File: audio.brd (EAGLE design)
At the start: 64.8 x 36.8 mm, 42 parts, among them CN1 PH-1X06SG, CN2 PH-1X06RG, CN3 STEREO-3.5-MJ8435, CN4 STEREO-3.5-MJ8435, CN5 DC-JACK-18742, IC1 R5F104BCAFP, IC2 NJM2746E, IC3 NJM2746E, IC4 VBT1-S5-S5-SMT, IC5 NJM2866F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

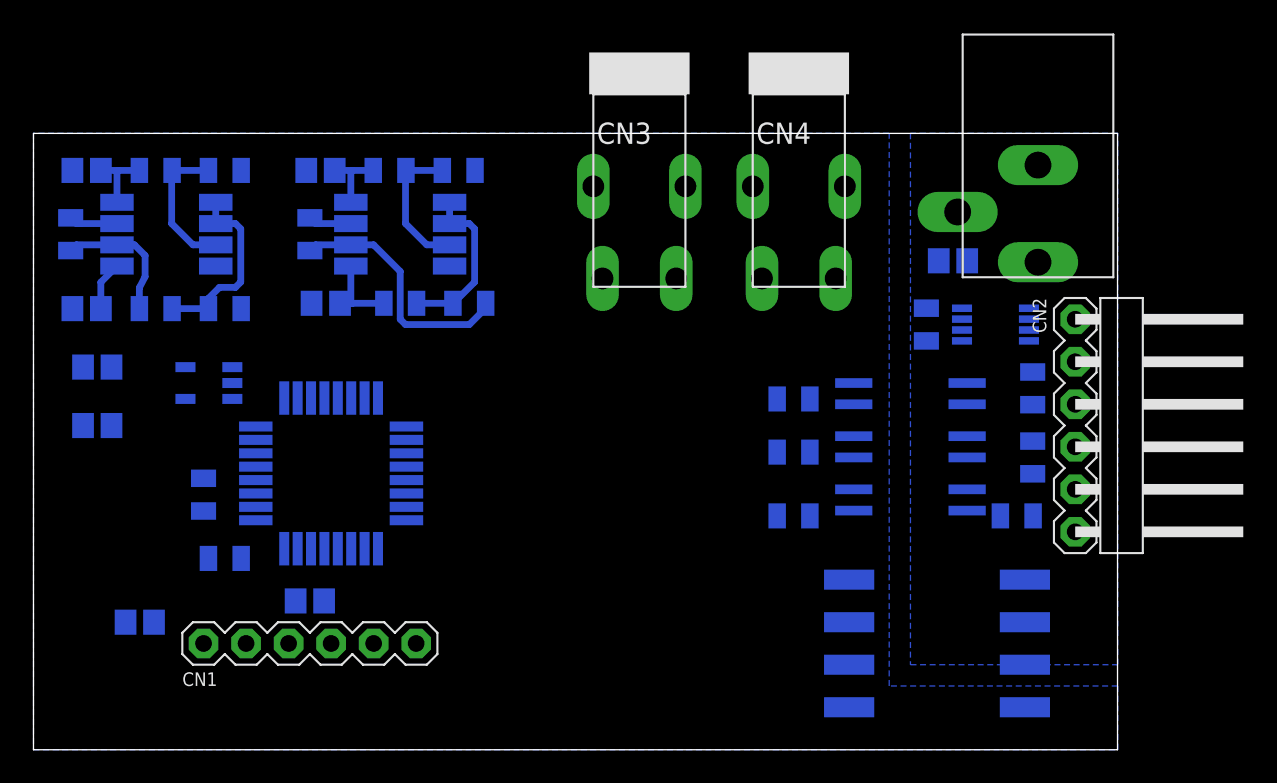
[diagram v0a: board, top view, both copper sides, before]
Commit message: Added power chains
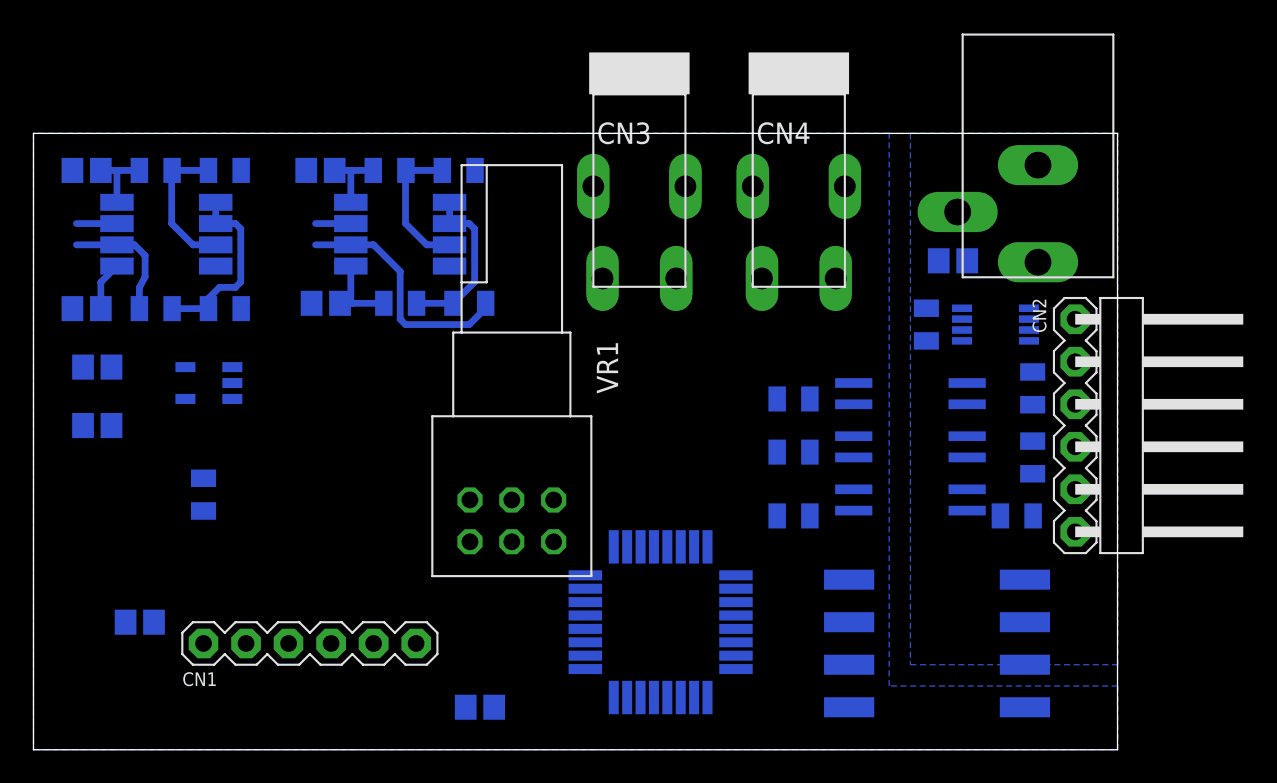
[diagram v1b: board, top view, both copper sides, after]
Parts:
- removed IC1: R5F104BCAFP, MyLib:P-LQFP32-7X7-0.80
- removed R1: 4.7k, MyLib:R2012
- removed R11, R12: 10k, MyLib:R2012
- added IC7: STM32F303K8T6, MyLib:P-LQFP32-7X7-0.80
- added VR1: (no value), MyLib:RK0971220-F15-C0-A104
- C1: value 1u -> 0.1u
- moved C1 12.0 mm to (26.7, 2.54)
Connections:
- net +3V3: now also C1.1, IC7.1, IC7.17, IC7.5; no longer IC1.8, R1.1, R2.1
- net GND: now also IC7.16, IC7.32, R2.1; no longer IC1.3, IC1.4, IC1.5, IC1.7
- net N$10: now also VR1.A3; no longer IC1.28, R11.2
- net N$14: now also VR1.B2; no longer R12.1
- net N$16: now also VR1.B3; no longer IC1.29, R12.2
- net N$17: no longer IC1.24
- net N$18: no longer IC1.23
- net N$19: no longer IC1.22
- net N$2: now also IC7.31, R2.2; no longer C1.1, IC1.6
- net N$4: no longer IC1.16
- net N$9: now also VR1.A2; no longer R11.1
- net RESET: no longer IC1.2, R2.2
- net TOOL0: no longer IC1.1, IC1.15, R1.2
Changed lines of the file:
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@@
 </autorouter>
 <elements>
-<element name="C1" library="MyLib" package="C2012" value="1u" x="16.51" y="8.89" rot="MR0"/>
 <element name="C2" library="MyLib" package="C2012" value="0.1u" x="6.35" y="7.62" rot="MR0"/>
 <element name="CN2" library="MyLib" package="PH-1X06RG" value="PH-1X06RG" x="62.23" y="19.3675" rot="R270"/>
-<element name="IC1" library="MyLib" package="P-LQFP32-7X7-0.80" value="R5F104BCAFP" x="17.78" y="16.51" rot="MR0"/>
 <element name="IC2" library="MyLib" package="EMP8" value="NJM2746E" x="21.9075" y="30.7975" rot="MR0"/>
-<element name="R1" library="MyLib" package="R2012" value="4.7k" x="11.43" y="11.43" rot="MR0"/>
 <element name="R2" library="MyLib" package="R2012" value="47k" x="10.16" y="15.24" rot="MR270"/>
 <element name="CN3" library="MyLib" package="MJ8435" value="STEREO-3.5-MJ8435" x="36.195" y="33.655"/>
@@
 <element name="C7" library="MyLib" package="C2012" value="0.1u" x="3.175" y="34.6075" rot="MR0"/>
 <element name="C8" library="MyLib" package="C2012" value="0.1u" x="17.145" y="34.6075" rot="MR0"/>
-<element name="R11" library="MyLib" package="R2012" value="10k" x="16.51" y="30.7975" rot="MR90"/>
-<element name="R12" library="MyLib" package="R2012" value="10k" x="2.2225" y="30.7975" rot="MR90"/>
 <element name="R13" library="MyLib" package="R2012" value="1k" x="45.4025" y="17.78" rot="MR180"/>
 <element name="R14" library="MyLib" package="R2012" value="100" x="45.4025" y="20.955" rot="MR180"/>
@@
 <element name="C9" library="MyLib" package="C2012" value="0.1u" x="54.9275" y="29.21" rot="MR0"/>
 <element name="R19" library="MyLib" package="R2012" value="4.7k" x="59.69" y="17.4625" rot="MR270"/>
+<element name="VR1" library="MyLib" package="RK0971220-F15-C0-A104" value="" x="28.575" y="14.9225"/>
+<element name="IC7" library="MyLib" package="P-LQFP32-7X7-0.80" value="STM32F303K8T6" x="37.465" y="7.62" rot="MR0"/>
+<element name="C1" library="MyLib" package="C2012" value="0.1u" x="26.67" y="2.54" rot="MR0"/>
 </elements>
 <signals>
@@
 <wire x1="4.66" y1="22.86" x2="11.8775" y2="22.8575" width="0" layer="19" extent="16-16"/>
 </signal>
-<signal name="N$2">
-<contactref element="IC1" pad="6"/>
-<contactref element="C1" pad="1"/>
-<wire x1="17.36" y1="8.89" x2="16.58" y2="12.01" width="0" layer="19" extent="16-16"/>
-</signal>
 <signal name="GND">
-<contactref element="IC1" pad="7"/>
-<contactref element="C2" pad="2"/>
-<contactref element="C1" pad="2"/>
-<contactref element="IC1" pad="3"/>
-<contactref element="IC1" pad="4"/>
-<contactref element="IC1" pad="5"/>
 <contactref element="CN1" pad="P$6"/>
 <contactref element="IC5" pad="P$2"/>
@@
 <vertex x="0" y="36.83"/>
 </polygon>
+<contactref element="IC7" pad="32"/>
+<contactref element="IC7" pad="16"/>
+<contactref element="R2" pad="1"/>
+<contactref element="C2" pad="2"/>
+<contactref element="C1" pad="2"/>
 </signal>
 <signal name="N$4">
-<contactref element="IC1" pad="16"/>
 <contactref element="CN1" pad="P$2"/>
-<wire x1="12.7" y1="6.35" x2="13.28" y2="19.31" width="0" layer="19" extent="16-16"/>
 </signal>
 <signal name="TOOL0">
-<contactref element="IC1" pad="15"/>
-<contactref element="R1" pad="2"/>
-<contactref element="IC1" pad="1"/>
 <contactref element="CN1" pad="P$3"/>
-<wire x1="10.453" y1="11.43" x2="13.28" y2="18.51" width="0" layer="19" extent="16-16"/>
-<wire x1="15.24" y1="6.35" x2="10.453" y2="11.43" width="0" layer="19" extent="16-16"/>
-<wire x1="20.58" y1="12.01" x2="15.24" y2="6.35" width="0" layer="19" extent="16-16"/>
 </signal>
 <signal name="RESET">
-<contactref element="R2" pad="2"/>
-<contactref element="IC1" pad="2"/>
 <contactref element="CN1" pad="P$5"/>
-<wire x1="20.32" y1="6.35" x2="19.78" y2="12.01" width="0" layer="19" extent="16-16"/>
-<wire x1="10.16" y1="14.263" x2="19.78" y2="12.01" width="0" layer="19" extent="16-16"/>
 </signal>
 <signal name="N$3">
@@
 </signal>
 <signal name="+3V3">
-<contactref element="IC1" pad="8"/>
-<contactref element="C2" pad="1"/>
-<contactref element="R2" pad="1"/>
-<contactref element="R1" pad="1"/>
 <contactref element="IC5" pad="P$5"/>
 <contactref element="C6" pad="1"/>
@@
 <wire x1="4.9875" y1="32.7025" x2="4.9875" y2="34.515" width="0.4064" layer="16"/>
 <wire x1="4.9875" y1="34.515" x2="5.08" y2="34.6075" width="0.4064" layer="16"/>
-<wire x1="20.2955" y1="34.6075" x2="44.4255" y2="17.78" width="0" layer="19" extent="16-16"/>
-<wire x1="6.3255" y1="34.6075" x2="17.995" y2="34.6075" width="0" layer="19" extent="16-16"/>
-<wire x1="9.0775" y1="22.8575" x2="4.9875" y2="32.7025" width="0" layer="19" extent="16-16"/>
-<wire x1="4.66" y1="19.3675" x2="9.0775" y2="22.8575" width="0" layer="19" extent="16-16"/>
-<wire x1="10.16" y1="16.217" x2="4.66" y2="19.3675" width="0" layer="19" extent="16-16"/>
-<wire x1="12.407" y1="11.43" x2="10.16" y2="16.217" width="0" layer="19" extent="16-16"/>
-<wire x1="14.98" y1="12.01" x2="12.407" y2="11.43" width="0" layer="19" extent="16-16"/>
-<wire x1="7.2" y1="7.62" x2="12.407" y2="11.43" width="0" layer="19" extent="16-16"/>
+<contactref element="IC7" pad="1"/>
+<contactref element="IC7" pad="5"/>
+<contactref element="C2" pad="1"/>
+<contactref element="IC7" pad="17"/>
+<contactref element="C1" pad="1"/>
+<wire x1="34.665" y1="12.12" x2="44.4255" y2="17.78" width="0" layer="19" extent="16-16"/>
+<wire x1="37.065" y1="3.12" x2="34.665" y2="12.12" width="0" layer="19" extent="16-16"/>
+<wire x1="40.265" y1="3.12" x2="37.065" y2="3.12" width="0" layer="19" extent="16-16"/>
+<wire x1="27.52" y1="2.54" x2="37.065" y2="3.12" width="0" layer="19" extent="16-16"/>
+<wire x1="7.2" y1="7.62" x2="27.52" y2="2.54" width="0" layer="19" extent="16-16"/>
+<wire x1="4.66" y1="19.3675" x2="7.2" y2="7.62" width="0" layer="19" extent="16-16"/>
+<wire x1="9.0775" y1="22.8575" x2="4.66" y2="19.3675" width="0" layer="19" extent="16-16"/>
+<wire x1="4.9875" y1="32.7025" x2="9.0775" y2="22.8575" width="0" layer="19" extent="16-16"/>
+<wire x1="17.995" y1="34.6075" x2="6.3255" y2="34.6075" width="0" layer="19" extent="16-16"/>
 </signal>
 <signal name="N$7">
@@
 <contactref element="R5" pad="2"/>
 <contactref element="IC2" pad="P$6"/>
-<contactref element="R11" pad="1"/>
 <wire x1="18.9575" y1="30.1625" x2="16.852" y2="30.1625" width="0.4064" layer="16"/>
-<wire x1="16.852" y1="30.1625" x2="16.51" y2="29.8205" width="0.4064" layer="16"/>
 <wire x1="18.9575" y1="30.1625" x2="20.32" y2="30.1625" width="0.4064" layer="16"/>
 <wire x1="20.32" y1="30.1625" x2="21.9075" y2="28.575" width="0.4064" layer="16"/>
@@
 <wire x1="22.225" y1="25.4" x2="21.9075" y2="25.7175" width="0.4064" layer="16"/>
 <wire x1="21.9075" y1="25.7175" x2="21.9075" y2="28.575" width="0.4064" layer="16"/>
+<contactref element="VR1" pad="A2"/>
+<wire x1="28.575" y1="14.9225" x2="26.035" y2="25.4" width="0" layer="19" extent="16-16"/>
 </signal>
 <signal name="N$10">
 <contactref element="IC2" pad="P$7"/>
-<contactref element="R11" pad="2"/>
-<contactref element="IC1" pad="28"/>
 <wire x1="18.9575" y1="31.4325" x2="16.852" y2="31.4325" width="0.4064" layer="16"/>
-<wire x1="16.852" y1="31.4325" x2="16.51" y2="31.7745" width="0.4064" layer="16"/>
-<wire x1="22.28" y1="16.91" x2="18.9575" y2="31.4325" width="0" layer="19" extent="16-16"/>
+<contactref element="VR1" pad="A3"/>
+<wire x1="26.075" y1="14.9225" x2="18.9575" y2="31.4325" width="0" layer="19" extent="16-16"/>
 </signal>
 <signal name="N$14">
 <contactref element="IC3" pad="P$6"/>
 <contactref element="R9" pad="2"/>
-<contactref element="R12" pad="1"/>
 <wire x1="4.9875" y1="30.1625" x2="2.5645" y2="30.1625" width="0.4064" layer="16"/>
-<wire x1="2.5645" y1="30.1625" x2="2.2225" y2="29.8205" width="0.4064" layer="16"/>
 <wire x1="6.3255" y1="26.3525" x2="6.3255" y2="27.598" width="0.4064" layer="16"/>
 <wire x1="6.3255" y1="27.598" x2="6.6675" y2="28.2575" width="0.4064" layer="16"/>
@@
 <wire x1="6.6675" y1="29.5275" x2="6.0325" y2="30.1625" width="0.4064" layer="16"/>
 <wire x1="6.0325" y1="30.1625" x2="4.9875" y2="30.1625" width="0.4064" layer="16"/>
+<contactref element="VR1" pad="B2"/>
+<wire x1="6.3255" y1="26.3525" x2="28.575" y2="12.4225" width="0" layer="19" extent="16-16"/>
 </signal>
 <signal name="N$16">
 <contactref element="IC3" pad="P$7"/>
-<contactref element="R12" pad="2"/>
-<contactref element="IC1" pad="29"/>
 <wire x1="4.9875" y1="31.4325" x2="2.5645" y2="31.4325" width="0.4064" layer="16"/>
-<wire x1="2.5645" y1="31.4325" x2="2.2225" y2="31.7745" width="0.4064" layer="16"/>
-<wire x1="4.9875" y1="31.4325" x2="22.28" y2="16.11" width="0" layer="19" extent="16-16"/>
+<contactref element="VR1" pad="B3"/>
+<wire x1="4.9875" y1="31.4325" x2="26.075" y2="12.4225" width="0" layer="19" extent="16-16"/>
 </signal>
 <signal name="N$17">
-<contactref element="IC1" pad="24"/>
 <contactref element="R14" pad="1"/>
-<wire x1="20.58" y1="21.01" x2="44.4255" y2="20.955" width="0" layer="19" extent="16-16"/>
 </signal>
 <signal name="N$18">
 <contactref element="U$2" pad="P$4"/>
-<contactref element="IC1" pad="23"/>
 <contactref element="R13" pad="2"/>
 <wire x1="46.3795" y1="17.78" x2="49" y2="18.7325" width="0" layer="19" extent="16-16"/>
-<wire x1="19.78" y1="21.01" x2="46.3795" y2="17.78" width="0" layer="19" extent="16-16"/>
 </signal>
 <signal name="N$19">
-<contactref element="IC1" pad="22"/>
 <contactref element="R15" pad="1"/>
-<wire x1="18.98" y1="21.01" x2="44.4255" y2="13.97" width="0" layer="19" extent="16-16"/>
 </signal>
 <signal name="N$20">
@@
 <wire x1="55.4675" y1="25.075" x2="59.69" y2="22.567" width="0" layer="19" extent="16-16"/>
 </signal>
+<signal name="N$2">
+<contactref element="IC7" pad="31"/>
+<contactref element="R2" pad="2"/>
+<wire x1="10.16" y1="14.263" x2="41.965" y2="5.62" width="0" layer="19" extent="16-16"/>
+</signal>
 </signals>
